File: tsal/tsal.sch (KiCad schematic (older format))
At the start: 22 parts, among them J1 Indicator, J2 GLV, J3 TSAL, P1 TS+ (PreAIR), P2 TS-, P3 TS+ (PostAIR), Q1 Q_PMOS_GSD, U1 V7812W-500, U2 TL431, U3 TCMT1103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

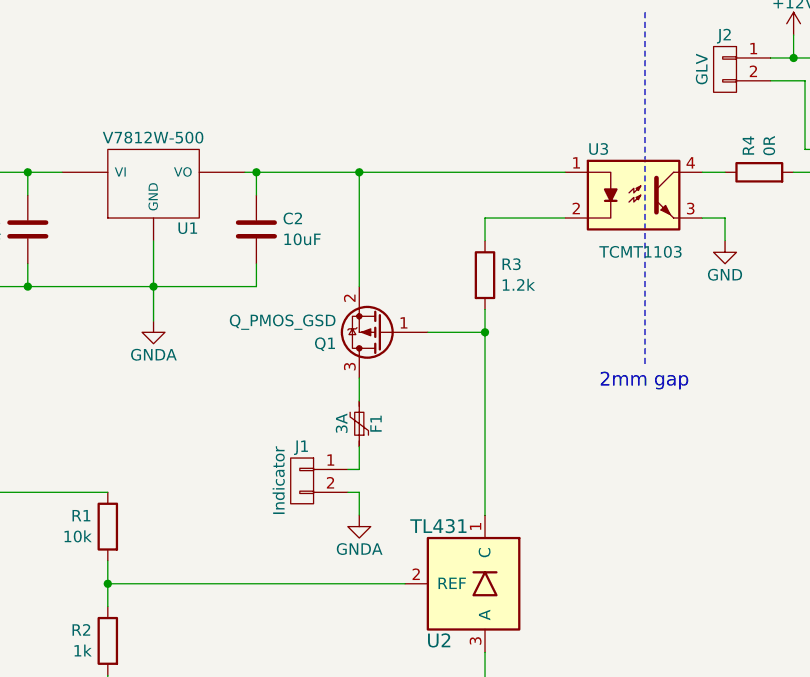
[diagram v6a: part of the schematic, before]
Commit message: Changed position of resistor
The P-FET will now turn off reliably.
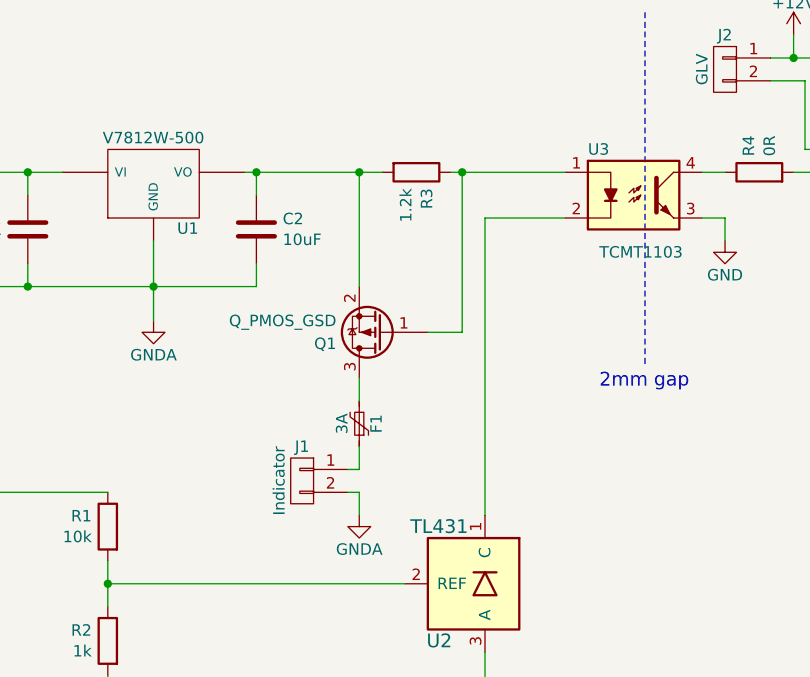
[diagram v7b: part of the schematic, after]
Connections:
- net at C2.1, Q1.2 (S), U1.3 (VO): now also R3.2; no longer U3.1
- net at U3.2: now also U2.1 (C); no longer R3.1
- new net: Q1.1 (G), R3.1, U3.1
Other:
- moved on the sheet: R3
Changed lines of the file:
@@
 L R R3
 U 1 1 58CB3E27
-P 5500 2950
-F 0 "R3" H 5570 2996 50  0000 L CNN
-F 1 "1.2k" H 5570 2905 50  0000 L CNN
-F 2 "Resistors_SMD:R_0805_HandSoldering" V 5430 2950 50  0001 C CNN
-F 3 "" H 5500 2950 50  0000 C CNN
-	1    5500 2950
-	1    0    0    -1
+P 5200 2500
+F 0 "R3" H 5270 2546 50  0000 L CNN
+F 1 "1.2k" H 5270 2455 50  0000 L CNN
+F 2 "Resistors_SMD:R_0805_HandSoldering" V 5130 2500 50  0001 C CNN
+F 3 "" H 5200 2500 50  0000 C CNN
+	1    5200 2500
+	0    1    1    0
 $EndComp
 $Comp
@@
 Wire Wire Line
 	6750 2000 7250 2000
-Connection ~ 5500 3200
-Wire Wire Line
-	5500 3100 5500 4000
+Wire Wire Line
+	5500 2700 5500 4000
 Wire Wire Line
 	8350 2400 8500 2400
 Wire Wire Line
 	7900 2400 8150 2400
-Wire Wire Line
-	5500 2700 5500 2800
 Connection ~ 3500 3000
 Wire Wire Line
@@
 	4050 2800 4050 3150
 Wire Wire Line
-	4450 2500 5850 2500
-Wire Wire Line
 	6550 2700 6550 2800
 Wire Wire Line
@@
 	8400 2650 8400 2500
 Wire Wire Line
-	5500 3200 5250 3200
-Wire Wire Line
-	4950 3000 4950 2500
+	4950 2500 4950 3000
 Connection ~ 4950 2500
 Wire Wire Line
@@
 Text Notes 6000 3450 0    60   ~ 0
 2mm gap
+Wire Wire Line
+	5400 2500 5400 3200
+Wire Wire Line
+	5400 3200 5250 3200
+Wire Wire Line
+	5350 2500 5850 2500
+Connection ~ 5400 2500
+Wire Wire Line
+	4450 2500 5050 2500
 $EndSCHEMATC
